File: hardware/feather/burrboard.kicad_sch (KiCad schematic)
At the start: 30 parts, among them J1 J1, J2 J2, J3 Conn_01x02_Male, Q1 TEMT6000X01, U1 TMP36, U2 ADXL345BCCZ

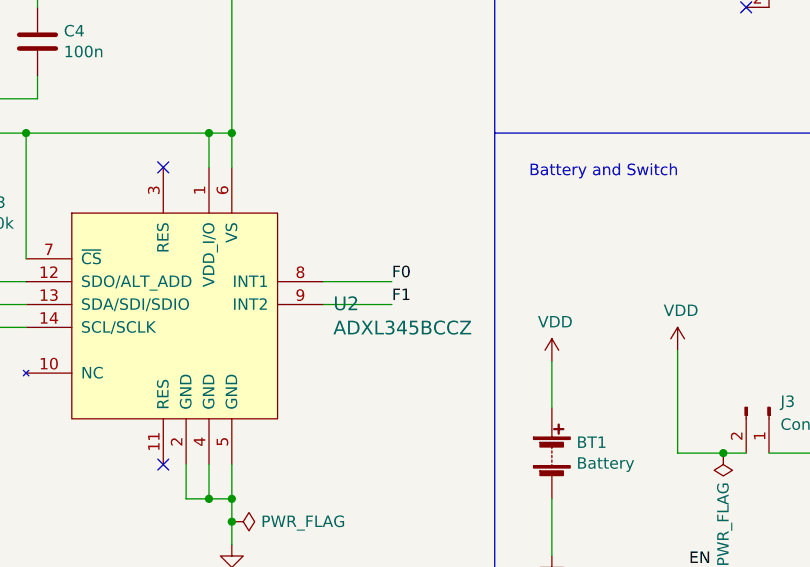
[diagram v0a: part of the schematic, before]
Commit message: Rotate accelerometer to match sense
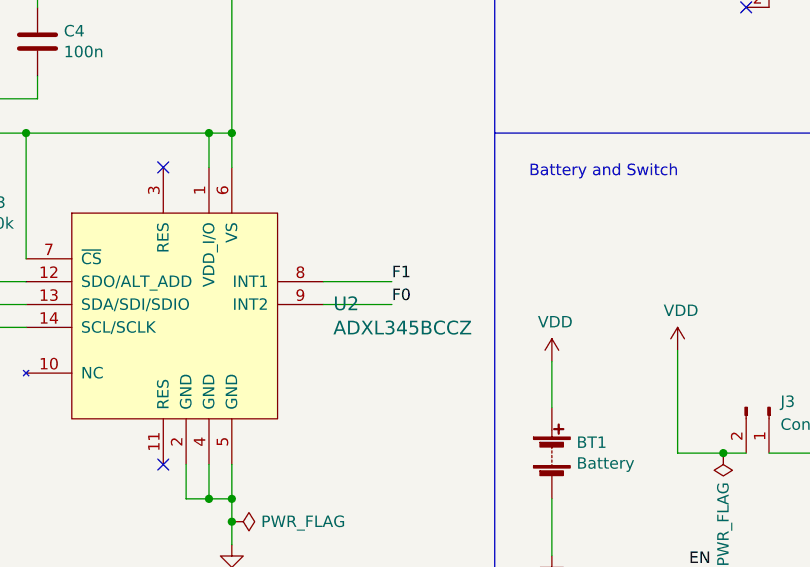
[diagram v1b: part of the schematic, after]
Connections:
- net F0: now also U2.9 (INT2); no longer U2.8 (INT1)
- net F1: now also U2.8 (INT1); no longer U2.9 (INT2)
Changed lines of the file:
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@@
     (effects (font (size 1.27 1.27)) (justify left bottom))
   )
-  (label "F1" (at 95.25 156.21 0)
+  (label "F0" (at 95.25 156.21 0)
     (effects (font (size 1.27 1.27)) (justify left bottom))
   )
@@
     (effects (font (size 1.27 1.27)) (justify left bottom))
   )
-  (label "F0" (at 95.25 153.67 0)
+  (label "F1" (at 95.25 153.67 0)
     (effects (font (size 1.27 1.27)) (justify left bottom))
   )

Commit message: Fix
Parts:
- C5: AISLER_MPN VJ0805A100JXAAC -> CL21B103KBANNNC; Digi-Key_PN 720-1699-2-ND -> 1276-1015-2-ND; MPN VJ0805A100JXAAC -> CL21B103KBANNNC; Manufacturer Vishay Vitramon -> Samsung Electro-Mechanics
- R7: value 680 -> 1.5k; AISLER_MPN RMCF0805FT680R -> RMCF0805FT1K50; Digi-Key_PN RMCF0805FT680RTR-ND -> RMCF0805FT1K50TR-ND; MPN RMCF0805FT680R -> RMCF0805FT1K50
- S1, S2: AISLER_MPN PTS645SM43SMTR92 LFS -> PTS645SK43SMTR92 LFS; DK_Detail_Page /product-detail/en/c-k/PTS645SM43SMTR92-LFS/CKN9112CT-ND/11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 -> https://www.digikey.no/no/products/detail/c-k/PTS645SK43SMT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; Digi-Key_PN CKN9112CT-ND -> CKN9084TR-ND; MPN PTS645SM43SMTR92 LFS -> PTS645SK43SMTR92 LFS
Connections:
- net EN: no longer S3.2 (B)
- net GND: no longer S3.3 (C)
- net VUSB: now also S3.1 (A); no longer J3.1 (Pin_1)
- new net: J3.1 (Pin_1), S3.2 (B)
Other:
- moved on the sheet: S3

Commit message: Rework design
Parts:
- removed C2: 10u, Capacitor_SMD:C_0805_2012Metric, symbol Device:C
- removed C3, C4: 100n, Capacitor_SMD:C_0805_2012Metric, symbol Device:C
- removed R3: 10k, Resistor_SMD:R_0805_2012Metric, symbol Device:R
- removed R9: 680, Resistor_SMD:R_0805_2012Metric, symbol Device:R
- removed U2: ADXL345BCCZ, burrboard:LGA-14_3x5mm_RevA, symbol burrboard:ADXL345BCCZ
- R2: value 10k -> 1.5k; AISLER_MPN RMCF0805FT10K0 -> RMCF0805FT1K50; Digi-Key_PN RMCF0805FT10K0TR-ND -> RMCF0805FT1K50TR-ND; MPN RMCF0805FT10K0 -> RMCF0805FT1K50
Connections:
- net 3V3: no longer R2.1
- net A2: now also R6.2; no longer R7.2
- net A3: now also R7.2
- net A4: now also R2.2; no longer R8.2
- net F2: now also R8.2; no longer R5.1, S2.1
- net F3: now also R5.1, S2.1; no longer R4.1, S1.1
- net F4: now also R4.1, S1.1; no longer R6.2
- net at D3.2 (A): now also R2.1
- net EN: no longer names the net of J2.11 (Pin_11)
- net F0: no longer names the net of J2.3 (Pin_3)
- net F1: no longer names the net of J2.4 (Pin_4)
- net SCL: no longer names the net of J2.2 (Pin_2)
- net SDA: no longer names the net of J2.1 (Pin_1)
- net SDA: no longer R2.2
- no-connect marks 19 -> 22
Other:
- note removed: "Accelerometer"

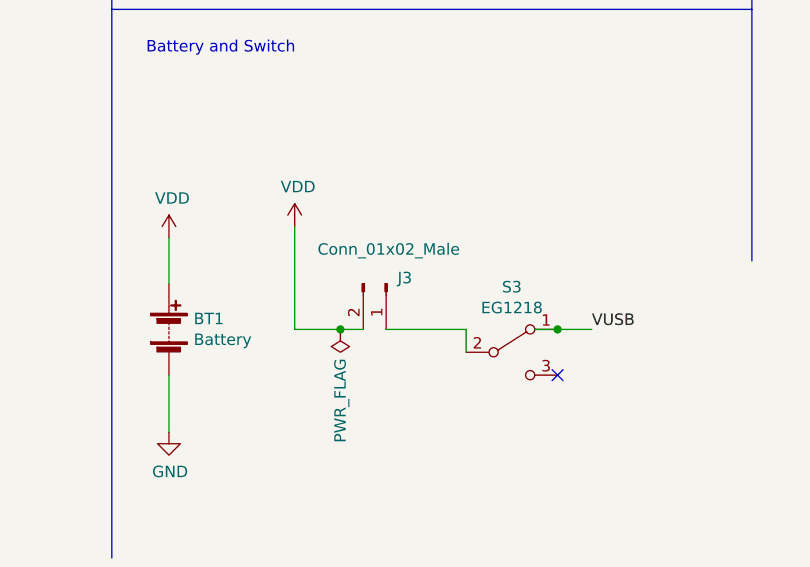
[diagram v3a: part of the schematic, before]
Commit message: Make space for QR code
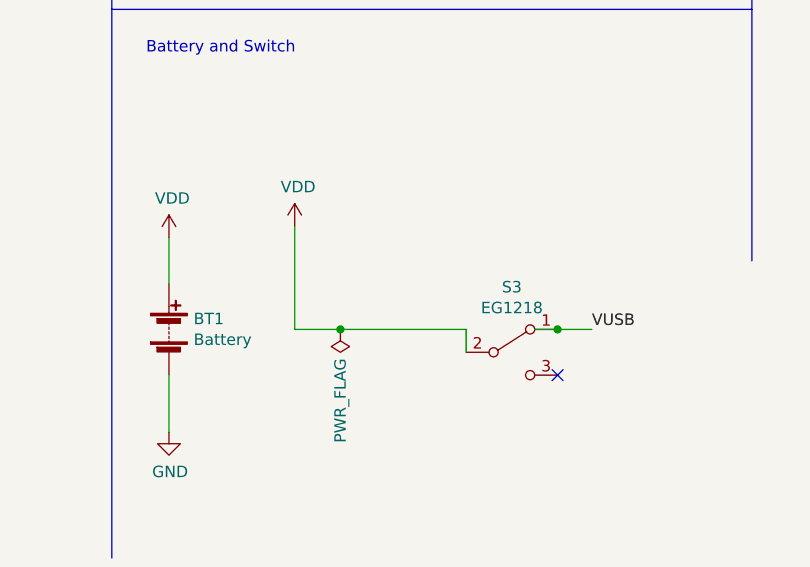
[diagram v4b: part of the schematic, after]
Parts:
- removed J3: Conn_01x02_Male, Connector_PinHeader_2.54mm:PinHeader_1x02_P2.54mm_Vertical, symbol Connector:Conn_01x02_Male
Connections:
- net VDD: now also S3.2 (B)
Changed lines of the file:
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@@
   (title_block
     (title "Drogue IoT BurrBoard")
-    (date "2022-01-13")
-    (rev "v2.0")
+    (date "2022-01-26")
+    (rev "v3.0")
     (company "Red Hat")
     (comment 2 "https://apache.org/licenses/LICENSE-2.0")
@@
     (stroke (width 0) (type default) (color 0 0 0 0))
   )
-  (wire (pts (xy 132.08 172.72) (xy 134.62 172.72))
-    (stroke (width 0) (type default) (color 0 0 0 0))
-  )
   (wire (pts (xy 68.58 52.07) (xy 82.55 52.07))
     (stroke (width 0) (type default) (color 0 0 0 0))
@@
     (stroke (width 0) (type default) (color 0 0 0 0))
   )
-  (wire (pts (xy 137.16 172.72) (xy 146.05 172.72))
+  (wire (pts (xy 132.08 172.72) (xy 146.05 172.72))
     (stroke (width 0) (type default) (color 0 0 0 0))
   )
@@
     (pin "1")
   )
-  (symbol (lib_id "Connector:Conn_01x02_Male") (at 137.16 167.64 270) (unit 1)
-    (in_bom yes) (on_board yes)
-    (property "Reference" "J3" (id 0) (at 138.43 167.0049 90)
-      (effects (font (size 1.27 1.27)) (justify left))
-    )
-    (property "Value" "Conn_01x02_Male" (id 1) (at 129.54 163.83 90)
-      (effects (font (size 1.27 1.27)) (justify left))
-    )
-    (property "Footprint" "Connector_PinHeader_2.54mm:PinHeader_1x02_P2.54mm_Vertical" (id 2) (at 137.16 167.64 0)
-      (effects (font (size 1.27 1.27)) hide)
-    )
-    (property "Datasheet" "~" (id 3) (at 137.16 167.64 0)
-      (effects (font (size 1.27 1.27)) hide)
-    )
-    (property "MPN" "77311-118-02LF" (id 4) (at 137.16 167.64 90)
-      (effects (font (size 1.27 1.27)) hide)
-    )
-    (property "AISLER_MPN" "77311-118-02LF" (id 5) (at 137.16 167.64 90)
-      (effects (font (size 1.27 1.27)) hide)
-    )
-    (property "Manufacturer" "Amphenol" (id 6) (at 137.16 167.64 90)
-      (effects (font (size 1.27 1.27)) hide)
-    )
-    (property "Digi-Key_PN" "609-4434-ND" (id 7) (at 137.16 167.64 90)
-      (effects (font (size 1.27 1.27)) hide)
-    )
-    (pin "1")
-    (pin "2")
-  )
   (symbol (lib_id "power:PWR_FLAG") (at 55.88 63.5 270) (unit 1)
     (in_bom yes) (on_board yes) (fields_autoplaced)
@@
       (reference "J2") (unit 1) (value "J2") (footprint "Connector_PinSocket_2.54mm:PinSocket_1x12_P2.54mm_Vertical")
     )
-    (path "/356a24f9-7ddf-40bf-8ee9-b7ec45ae0f65"
-      (reference "J3") (unit 1) (value "Conn_01x02_Male") (footprint "Connector_PinHeader_2.54mm:PinHeader_1x02_P2.54mm_Vertical")
-    )
     (path "/666dc925-2b95-4de4-a148-45e51fb4be3f"

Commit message: Update
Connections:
- net VDD: no longer R10.2
- net VUSB: now also R10.2
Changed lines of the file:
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@@
     (effects (font (size 1.27 1.27)) (justify left bottom))
+  )
+  (label "VUSB" (at 109.22 25.4 180)
+    (effects (font (size 1.27 1.27)) (justify right bottom))
   )
   (label "A1" (at 224.79 40.64 0)
@@
     )
   )
-  (symbol (lib_id "power:VDD") (at 109.22 25.4 0) (unit 1)
-    (in_bom yes) (on_board yes)
-    (property "Reference" "#PWR08" (id 0) (at 109.22 29.21 0)
-      (effects (font (size 1.27 1.27)) hide)
-    )
-    (property "Value" "VDD" (id 1) (at 109.601 21.0058 0))
-    (property "Footprint" "" (id 2) (at 109.22 25.4 0)
-      (effects (font (size 1.27 1.27)) hide)
-    )
-    (property "Datasheet" "" (id 3) (at 109.22 25.4 0)
-      (effects (font (size 1.27 1.27)) hide)
-    )
-    (pin "1")
-  )
   (symbol (lib_id "power:PWR_FLAG") (at 55.88 63.5 270) (unit 1)
     (in_bom yes) (on_board yes) (fields_autoplaced)
@@
       (reference "#PWR07") (unit 1) (value "GND") (footprint "")
     )
-    (path "/30d56621-b469-406c-9984-c3e3f5682099"
-      (reference "#PWR08") (unit 1) (value "VDD") (footprint "")
-    )
     (path "/f382406d-81c4-43b6-97fa-b574d17e5924"

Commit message: Add changes to rev3
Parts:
- added J3: SWD, Connector_PinHeader_2.54mm:PinHeader_1x02_P2.54mm_Vertical, symbol Connector:Conn_01x02_Male
- added J4: SWDCLK, TestPoint:TestPoint_THTPad_D1.0mm_Drill0.5mm, symbol Connector:Conn_01x01_Male
- added J5: SWDIO, TestPoint:TestPoint_THTPad_D1.0mm_Drill0.5mm, symbol Connector:Conn_01x01_Male
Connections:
- new net: J3.1 (Pin_1), J4.1 (Pin_1)
- new net: J3.2 (Pin_2), J5.1 (Pin_1)
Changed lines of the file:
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@@
   (no_connect (at 134.62 95.25))
   (no_connect (at 250.19 40.64))
-  (no_connect (at 229.87 60.96))
   (no_connect (at 180.34 43.18))
   (no_connect (at 229.87 33.02))
@@
   (no_connect (at 229.87 53.34))
   (no_connect (at 229.87 55.88))
-  (no_connect (at 229.87 63.5))
   (no_connect (at 229.87 27.94))
   (no_connect (at 144.78 118.11))
@@
   (no_connect (at 250.19 60.96))
   (no_connect (at 250.19 45.72))
+  (no_connect (at 229.87 60.96))
+  (no_connect (at 229.87 63.5))
   (wire (pts (xy 146.05 172.72) (xy 146.05 175.26))
     (stroke (width 0) (type default) (color 0 0 0 0))
@@
     (stroke (width 0) (type default) (color 0 0 0 0))
   )
+  (wire (pts (xy 73.406 133.096) (xy 85.344 133.096))
+    (stroke (width 0) (type default) (color 0 0 0 0))
+  )
   (wire (pts (xy 113.03 162.56) (xy 113.03 167.64))
     (stroke (width 0) (type default) (color 0 0 0 0))
@@
   )
   (wire (pts (xy 204.47 116.84) (xy 204.47 124.46))
+    (stroke (width 0) (type default) (color 0 0 0 0))
+  )
+  (wire (pts (xy 73.406 130.556) (xy 85.344 130.556))
     (stroke (width 0) (type default) (color 0 0 0 0))
   )
@@
     )
   )
+  (symbol (lib_id "Connector:Conn_01x01_Male") (at 90.424 130.556 180) (unit 1)
+    (in_bom yes) (on_board yes)
+    (property "Reference" "J4" (id 0) (at 87.63 127.254 0))
+    (property "Value" "SWDCLK" (id 1) (at 94.996 130.556 0))
+    (property "Footprint" "TestPoint:TestPoint_THTPad_D1.0mm_Drill0.5mm" (id 2) (at 90.424 130.556 0)
+      (effects (font (size 1.27 1.27)) hide)
+    )
+    (property "Datasheet" "~" (id 3) (at 90.424 130.556 0)
+      (effects (font (size 1.27 1.27)) hide)
+    )
+    (pin "1")
+  )
   (symbol (lib_id "power:PWR_FLAG") (at 55.88 63.5 270) (unit 1)
     (in_bom yes) (on_board yes) (fields_autoplaced)
@@
     (pin "2")
   )
+  (symbol (lib_id "Connector:Conn_01x02_Male") (at 68.326 130.556 0) (unit 1)
+    (in_bom yes) (on_board yes) (fields_autoplaced)
+    (property "Reference" "J3" (id 0) (at 68.961 125.476 0))
+    (property "Value" "SWD" (id 1) (at 68.961 128.016 0))
+    (property "Footprint" "Connector_PinHeader_2.54mm:PinHeader_1x02_P2.54mm_Vertical" (id 2) (at 68.326 130.556 0)
+      (effects (font (size 1.27 1.27)) hide)
+    )
+    (property "Datasheet" "~" (id 3) (at 68.326 130.556 0)
+      (effects (font (size 1.27 1.27)) hide)
+    )
+    (pin "1")
+    (pin "2")
+  )
   (symbol (lib_id "Device:R") (at 130.81 52.07 180) (unit 1)
     (in_bom yes) (on_board yes)
@@
     (pin "1")
     (pin "2")
+  )
+  (symbol (lib_id "Connector:Conn_01x01_Male") (at 90.424 133.096 180) (unit 1)
+    (in_bom yes) (on_board yes)
+    (property "Reference" "J5" (id 0) (at 87.63 135.636 0))
+    (property "Value" "SWDIO" (id 1) (at 94.234 133.096 0))
+    (property "Footprint" "TestPoint:TestPoint_THTPad_D1.0mm_Drill0.5mm" (id 2) (at 90.424 133.096 0)
+      (effects (font (size 1.27 1.27)) hide)
+    )
+    (property "Datasheet" "~" (id 3) (at 90.424 133.096 0)
+      (effects (font (size 1.27 1.27)) hide)
+    )
+    (pin "1")
   )
   (symbol (lib_id "power:GND") (at 109.22 60.96 0) (unit 1)
@@
       (reference "J2") (unit 1) (value "J2") (footprint "Connector_PinSocket_2.54mm:PinSocket_1x12_P2.54mm_Vertical")
     )
+    (path "/7a96ea12-e031-49a1-a3a0-24202e6db0ee"
+      (reference "J3") (unit 1) (value "SWD") (footprint "Connector_PinHeader_2.54mm:PinHeader_1x02_P2.54mm_Vertical")
+    )
+    (path "/27a2e118-e759-4fab-964d-896d29cf8156"
+      (reference "J4") (unit 1) (value "SWDCLK") (footprint "TestPoint:TestPoint_THTPad_D1.0mm_Drill0.5mm")
+    )
+    (path "/d9d24c41-2b35-4b0c-8337-be81a29cea75"
+      (reference "J5") (unit 1) (value "SWDIO") (footprint "TestPoint:TestPoint_THTPad_D1.0mm_Drill0.5mm")
+    )
     (path "/666dc925-2b95-4de4-a148-45e51fb4be3f"

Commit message: Update board
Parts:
- removed J3: SWD, Connector_PinHeader_2.54mm:PinHeader_1x02_P2.54mm_Vertical, symbol Connector:Conn_01x02_Male
- added J3: SWD, Connector_PinHeader_2.54mm:PinHeader_1x04_P2.54mm_Vertical, symbol Connector:Conn_01x04_Male
- J4, J5: Digi-Key_PN (none) -> ED1122-ND; MPN (none) -> 0985-0-15-20-71-14-11-0; Url (none) -> https://www.digikey.no/en/products/detail/mill-max-manufact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
- Q1: Digi-Key_PN (none) -> 751-1055-2-ND; MPN (none) -> TEMT6000X01; Manufacturer_Part_Number TEMT6000X01 -> (none)
- R11: value 2M -> 1.3M; AISLER_MPN RC0805FR-072ML -> RC0805FR-071M3L; Digi-Key_PN 311-2.00MCRTR-ND -> 311-1.30MCRTR-ND; Digikey https://www.digikey.no/en/products/detail/panasonic-electro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 -> https://www.digikey.no/en/products/detail/yageo/RC0805FR-07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; MPN RC0805FR-072ML -> RC0805FR-071M3L
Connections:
- net 3V3: now also J3.1 (Pin_1); no longer C1.1, Q1.3 (C), U1.5 (~{SHUTDOWN}), U1.8 (+Vs)
- net GND: now also J3.4 (Pin_4)
- net F0: now reaches J2.3 (Pin_3)
- net F0: now also C1.1, U1.5 (~{SHUTDOWN}), U1.8 (+Vs)
- net F1: now reaches J2.4 (Pin_4)
- net F1: now also Q1.3 (C)
- net at J4.1 (Pin_1): now also J3.2 (Pin_2)
- net at J5.1 (Pin_1): now also J3.3 (Pin_3)
- no-connect marks 22 -> 20

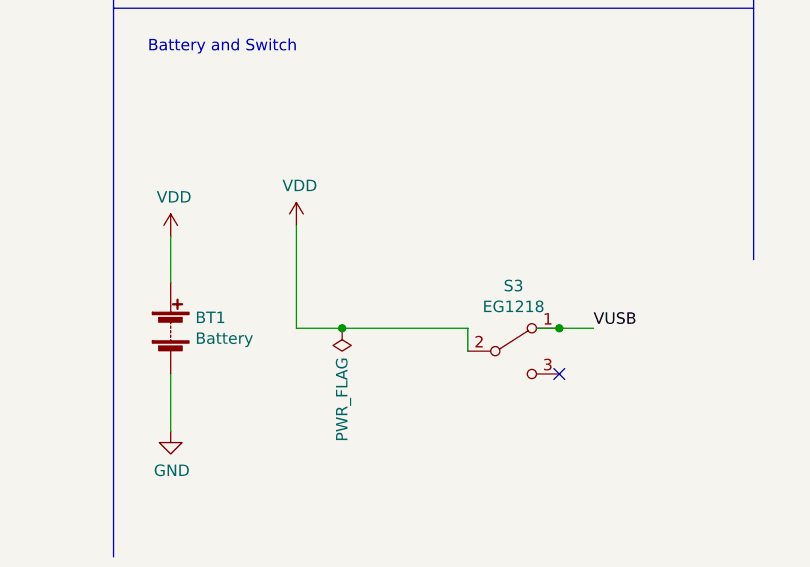
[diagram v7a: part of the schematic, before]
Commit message: Add schottky diode
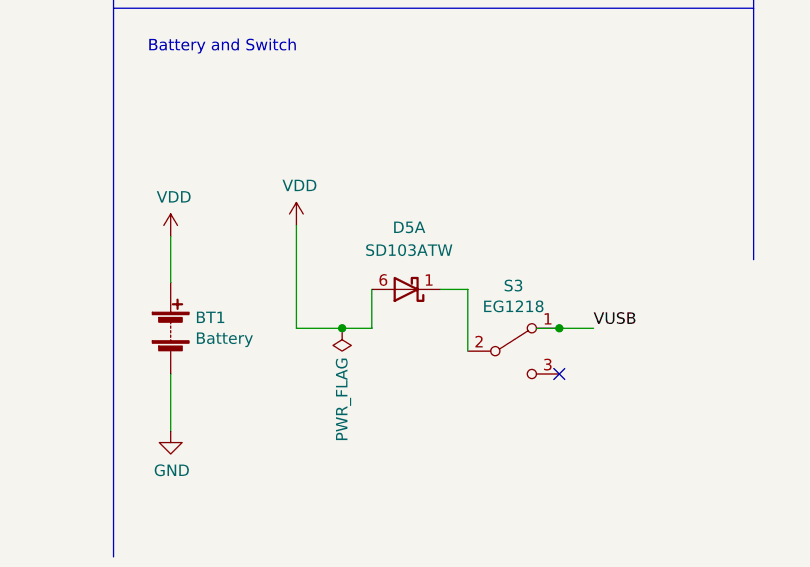
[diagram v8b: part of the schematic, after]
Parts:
- added D5: SD103ATW, Package_TO_SOT_SMD:SOT-363_SC-70-6, symbol Diode:SD103ATW
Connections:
- net VDD: now also D5.6 (A); no longer S3.2 (B)
- new net: D5.1 (K), S3.2 (B)
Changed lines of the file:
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@@
   (junction (at 236.22 143.51) (diameter 0) (color 0 0 0 0)
   )
+  (junction (at 130.81 44.45) (diameter 0) (color 0 0 0 0)
+  )
   (junction (at 132.08 172.72) (diameter 0) (color 0 0 0 0)
-  )
-  (junction (at 130.81 44.45) (diameter 0) (color 0 0 0 0)
   )
   (junction (at 55.88 63.5) (diameter 0) (color 0 0 0 0)
@@
   (no_connect (at 229.87 60.96))
   (no_connect (at 229.87 63.5))
-  (wire (pts (xy 146.05 172.72) (xy 146.05 175.26))
+  (wire (pts (xy 146.05 168.402) (xy 146.05 175.26))
     (stroke (width 0) (type default) (color 0 0 0 0))
   )
@@
     (stroke (width 0) (type default) (color 0 0 0 0))
   )
+  (wire (pts (xy 143.002 168.402) (xy 146.05 168.402))
+    (stroke (width 0) (type default) (color 0 0 0 0))
+  )
   (wire (pts (xy 27.94 38.1) (xy 43.18 38.1))
     (stroke (width 0) (type default) (color 0 0 0 0))
@@
     (stroke (width 0) (type default) (color 0 0 0 0))
   )
+  (wire (pts (xy 135.382 172.72) (xy 135.382 168.402))
+    (stroke (width 0) (type default) (color 0 0 0 0))
+  )
   (wire (pts (xy 187.96 132.08) (xy 187.96 143.51))
     (stroke (width 0) (type default) (color 0 0 0 0))
@@
     (stroke (width 0) (type default) (color 0 0 0 0))
   )
-  (wire (pts (xy 132.08 172.72) (xy 146.05 172.72))
-    (stroke (width 0) (type default) (color 0 0 0 0))
-  )
   (wire (pts (xy 220.98 38.1) (xy 220.98 35.56))
     (stroke (width 0) (type default) (color 0 0 0 0))
@@
   )
   (wire (pts (xy 273.05 91.44) (xy 273.05 109.22))
+    (stroke (width 0) (type default) (color 0 0 0 0))
+  )
+  (wire (pts (xy 132.08 172.72) (xy 135.382 172.72))
     (stroke (width 0) (type default) (color 0 0 0 0))
   )
@@
     (pin "1")
   )
+  (symbol (lib_id "Diode:SD103ATW") (at 139.192 168.402 180) (unit 1)
+    (in_bom yes) (on_board yes) (fields_autoplaced)
+    (property "Reference" "D5" (id 0) (at 139.5095 161.544 0))
+    (property "Value" "SD103ATW" (id 1) (at 139.5095 164.084 0))
+    (property "Footprint" "Package_TO_SOT_SMD:SOT-363_SC-70-6" (id 2) (at 139.192 163.322 0)
+      (effects (font (size 1.27 1.27)) hide)
+    )
+    (property "Datasheet" "https://www.diodes.com/assets/Datasheets/ds30374.pdf" (id 3) (at 139.192 168.402 0)
+      (effects (font (size 1.27 1.27)) hide)
+    )
+    (property "Manufacturer" "Diodes Incorporated" (id 4) (at 139.192 168.402 0)
+      (effects (font (size 1.27 1.27)) hide)
+    )
+    (property "Digi-Key_PN" "SD103ATW-FDITR-ND" (id 5) (at 139.192 168.402 0)
+      (effects (font (size 1.27 1.27)) hide)
+    )
+    (property "MPN" "SD103ATW-7-F" (id 6) (at 139.192 168.402 0)
+      (effects (font (size 1.27 1.27)) hide)
+    )
+    (pin "1")
+    (pin "6")
+  )
   (symbol (lib_id "Connector:Conn_01x04_Male") (at 59.436 130.556 0) (unit 1)
     (in_bom yes) (on_board yes) (fields_autoplaced)
@@
       (reference "D4") (unit 1) (value "YELLOW") (footprint "LED_SMD:LED_0805_2012Metric")
     )
+    (path "/ad2b492a-b87e-4f52-8b8e-ee061256242c"
+      (reference "D5") (unit 1) (value "SD103ATW") (footprint "Package_TO_SOT_SMD:SOT-363_SC-70-6")
+    )
     (path "/00000000-0000-0000-0000-00005d375c76"
